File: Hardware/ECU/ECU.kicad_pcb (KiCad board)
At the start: 2 copper layers, 0 parts

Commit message: PCB
Platine Vernetzt
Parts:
- added A1: Pololu_Breakout_DRV8825, Module:Pololu_Breakout-16_15.2x20.3mm, F.Cu at (173.5, 128.5)
- added BT1: Battery_Cell, 2999:BAT_2999, F.Cu at (154.5, 72.0)
- added C10: 1uF, Capacitor_SMD:C_0805_2012Metric, F.Cu at (111.4, 138.5)
- added C11: 1uF, Capacitor_SMD:C_0805_2012Metric, F.Cu at (200.8, 106.7)
- added C12: 0.1uF, Capacitor_SMD:C_0805_2012Metric, F.Cu at (194.2, 93.6)
- added C13: 0.1uF, Capacitor_SMD:C_0805_2012Metric, F.Cu at (96.0, 40.7)
- added C14: 0.1uF, Capacitor_SMD:C_0805_2012Metric, F.Cu at (73.5, 47.5)
- added C15: 270nF, Capacitor_SMD:C_0805_2012Metric, F.Cu at (96.0, 45.7)
- added C16: 0.22uF, Capacitor_SMD:C_0805_2012Metric, F.Cu at (92.4, 39.6)
- added C17: 0.22uF, Capacitor_SMD:C_0805_2012Metric, F.Cu at (70.0, 51.5)
- added C18: 270nF, Capacitor_SMD:C_0805_2012Metric, F.Cu at (73.0, 40.5)
- added C20: 0.1uF, Capacitor_SMD:C_0805_2012Metric, F.Cu at (92.5, 52.2)
- added C21: 0.1uF, Capacitor_SMD:C_0805_2012Metric, F.Cu at (102.0, 59.1)
- added C23: 0.1uF, Capacitor_SMD:C_0805_2012Metric, F.Cu at (91.5, 47.1)
- added C24: 0.22uF, Capacitor_SMD:C_0805_2012Metric, F.Cu at (92.6, 56.1)
- added C25: 0.22uF, Capacitor_SMD:C_0805_2012Metric, F.Cu at (97.0, 65.2)
- added C26: 0.1uF, Capacitor_SMD:C_0805_2012Metric, F.Cu at (117.2, 46.2)
- added C27: 100uF, Capacitor_SMD:C_1206_3216Metric, F.Cu at (123.9, 47.5)
- added C28: 0.22uF, Capacitor_SMD:C_0805_2012Metric, F.Cu at (117.2, 49.2)
- added C29: 0.01uF, Capacitor_SMD:C_0805_2012Metric, F.Cu at (119.4, 66.8)
- added C3: 0.1uF, Capacitor_SMD:C_0805_2012Metric, F.Cu at (83.5, 122.0)
- added C30: 0.01uF, Capacitor_SMD:C_0805_2012Metric, F.Cu at (119.4, 69.8)
- added C31: 100uF, Capacitor_SMD:CP_Elec_6.3x7.7, F.Cu at (182.3, 136.7)
- added C32: 0.1uF, Capacitor_SMD:C_0805_2012Metric, F.Cu at (96.0, 74.5)
- added C33: 47uF, Capacitor_Tantalum_SMD:CP_EIA-3528-21_Kemet-B, F.Cu at (93.0, 74.5)
- added C34: 0.1uF, Capacitor_SMD:C_0805_2012Metric, F.Cu at (95.5, 96.8)
- added C35: 22uF, Capacitor_SMD:CP_Elec_4x5.4, F.Cu at (79.0, 98.3)
- added C36: 47uF, Capacitor_Tantalum_SMD:CP_EIA-3528-21_Kemet-B, F.Cu at (95.5, 99.5)
- added C37: 0.1uF, Capacitor_SMD:C_0805_2012Metric, F.Cu at (73.5, 98.3)
- added C38: 33uF, Capacitor_SMD:CP_Elec_6.3x7.7, F.Cu at (73.0, 83.0)
- added C39: 33uF, Capacitor_SMD:CP_Elec_6.3x7.7, F.Cu at (73.0, 75.5)
- added C4: 0.01uF, Capacitor_SMD:C_0805_2012Metric, F.Cu at (75.7, 139.3)
- added C40: 0.1uF, Capacitor_SMD:C_0805_2012Metric, F.Cu at (73.2, 88.0)
- added C41: 0.1uF, Capacitor_SMD:C_0805_2012Metric, F.Cu at (92.5, 34.7)
- added C5: 4700pF, Capacitor_SMD:C_0805_2012Metric, F.Cu at (72.7, 139.3)
- added C6: 1nF, Capacitor_SMD:C_0805_2012Metric, F.Cu at (115.4, 132.5)
- added C7: 0.01uF, Capacitor_SMD:C_0805_2012Metric, F.Cu at (111.4, 133.5)
- added C8: 1nF, Capacitor_SMD:C_0805_2012Metric, F.Cu at (107.4, 132.6)
- added C9: 0.1uF, Capacitor_SMD:C_0805_2012Metric, F.Cu at (111.4, 136.0)
- added D1: LED, LED_SMD:LED_0805_2012Metric, F.Cu at (206.8, 62.4)
- added D11: D, Diode_SMD:D_SOD-323, F.Cu at (198.8, 65.8)
- added D13: D, Diode_SMD:D_SOD-323, F.Cu at (206.8, 65.8)
- added D15: D, Diode_SMD:D_SOD-323, F.Cu at (194.8, 65.8)
- added D18: LED, LED_SMD:LED_0805_2012Metric, F.Cu at (206.8, 69.2)
- added D19: LED, LED_SMD:LED_0805_2012Metric, F.Cu at (194.8, 69.2)
- added D2: LED, LED_SMD:LED_0805_2012Metric, F.Cu at (202.8, 62.4)
- added D21: LED, LED_SMD:LED_0805_2012Metric, F.Cu at (198.8, 62.4)
- added D22: LED, LED_SMD:LED_0805_2012Metric, F.Cu at (194.8, 62.4)
- added D25: D, Diode_SMD:D_SOD-323, F.Cu at (194.3, 128.9)
- added D26: D, Diode_SMD:D_SOD-323, F.Cu at (190.3, 128.9)
- added D27: D_Schottky, Diode_SMD:D_PowerDI-123, F.Cu at (155.5, 123.7)
- added D28: D, Diode_SMD:D_SOD-323, F.Cu at (202.8, 128.9)
- added D29: D, Diode_SMD:D_SOD-323, F.Cu at (198.8, 128.9)
- added D30: D, Diode_SMD:D_SOD-323, F.Cu at (185.8, 128.9)
- added D31: D, Diode_SMD:D_SOD-323, F.Cu at (181.8, 128.9)
- added D32: D_TVS, Diode_SMD:D_SMB, F.Cu at (73.2, 69.5)
- added D33: D_Schottky, Diode_SMD:D_SMA_Handsoldering, F.Cu at (79.5, 62.5)
- added D34: LED, LED_SMD:LED_0805_2012Metric_Pad1.15x1.40mm_HandSolder, F.Cu at (108.0, 104.0)
- added D35: LED, LED_SMD:LED_0805_2012Metric_Pad1.15x1.40mm_HandSolder, F.Cu at (105.5, 104.0)
- added D36: LED, LED_SMD:LED_0805_2012Metric_Pad1.15x1.40mm_HandSolder, F.Cu at (103.0, 104.0)
- added D37: D_Schottky, Diode_SMD:D_PowerDI-123, F.Cu at (145.5, 75.7)
- added D5: LED, LED_SMD:LED_0805_2012Metric, F.Cu at (202.8, 69.2)
- added D7: LED, LED_SMD:LED_0805_2012Metric, F.Cu at (198.8, 69.2)
- added D9: D, Diode_SMD:D_SOD-323, F.Cu at (202.8, 65.8)
- added F1: Polyfuse, Fuse:Fuse_1812_4532Metric, F.Cu at (184.3, 106.2)
- added F2: Polyfuse, Fuse:Fuse_0603_1608Metric, F.Cu at (94.0, 103.0)
- added IC1: MAX9926UAEE_V+, Package_SO:QSOP-16_3.9x4.9mm_P0.635mm, F.Cu at (111.5, 126.9)
- added IC2: ZXMS6006DT8, ZXMS6006DT8TA:SOT153P700X170-8N, F.Cu at (192.3, 123.4)
- added IC3: ZXMS6006DT8, ZXMS6006DT8TA:SOT153P700X170-8N, F.Cu at (183.8, 123.4)
- added IC4: ZXMS6006DT8, ZXMS6006DT8TA:SOT153P700X170-8N, F.Cu at (200.8, 123.4)
- added J1: Conn_01x04, Connector_PinHeader_2.54mm:PinHeader_1x04_P2.54mm_Vertical, F.Cu at (127.0, 80.2)
- added J5: ~, connector:6437288-3, F.Cu at (206.0, 36.5)
- added JP2: Jumper_2_Open, Jumper:SolderJumper-2_P1.3mm_Open_Pad1.0x1.5mm, F.Cu at (79.4, 110.0)
- added JP3: Jumper_2_Open, Jumper:SolderJumper-2_P1.3mm_Open_Pad1.0x1.5mm, F.Cu at (79.4, 122.0)
- added JP4: Jumper_2_Open, Jumper:SolderJumper-2_P1.3mm_Open_Pad1.0x1.5mm, F.Cu at (96.8, 103.5)
- added Q1: Q_DUAL_NMOS_S1G1D2S2G2D1, Package_TO_SOT_SMD:SOT-363_SC-70-6, F.Cu at (79.4, 116.3)
- added Q2: Q_DUAL_NMOS_S1G1D2S2G2D1, Package_TO_SOT_SMD:SOT-363_SC-70-6, F.Cu at (123.7, 67.3)
- added Q3: Q_PNP_BCEC, Package_TO_SOT_SMD:SOT-223-3_TabPin2, F.Cu at (89.0, 99.0)
- added R10: 1k, Resistor_SMD:R_0805_2012Metric, F.Cu at (202.8, 58.9)
- added R13: 1k, Resistor_SMD:R_0805_2012Metric, F.Cu at (202.8, 72.7)
- added R15: 1k, Resistor_SMD:R_0805_2012Metric, F.Cu at (198.8, 72.7)
- added R17: 10k, Resistor_SMD:R_0805_2012Metric, F.Cu at (199.4, 82.1)
- added R20: 1k, Resistor_SMD:R_0805_2012Metric, F.Cu at (206.8, 72.7)
- added R21: 1k, Resistor_SMD:R_0805_2012Metric, F.Cu at (194.8, 72.7)
- added R23: 1k, Resistor_SMD:R_0805_2012Metric, F.Cu at (198.8, 58.9)
- added R24: 1k, Resistor_SMD:R_0805_2012Metric, F.Cu at (194.8, 58.9)
- added R27: 604R, Resistor_SMD:R_0805_2012Metric, F.Cu at (73.6, 50.0)
- added R28: 3.88k, Resistor_SMD:R_0805_2012Metric_Pad1.20x1.40mm_HandSolder, F.Cu at (75.0, 58.5)
- added R29: 470R, Resistor_SMD:R_0805_2012Metric, F.Cu at (96.0, 38.2)
- added R3: 1k, Resistor_SMD:R_0805_2012Metric, F.Cu at (79.4, 113.0)
- added R30: 2.4k, Resistor_SMD:R_0805_2012Metric, F.Cu at (96.1, 43.7)
- added R31: 470R, Resistor_SMD:R_0805_2012Metric, F.Cu at (73.6, 54.5)
- added R32: 1k, Resistor_SMD:R_0805_2012Metric, F.Cu at (73.0, 34.5)
- added R33: 2.49k, Resistor_SMD:R_0805_2012Metric, F.Cu at (96.4, 52.2)
- added R34: 2.49k, Resistor_SMD:R_0805_2012Metric, F.Cu at (96.5, 60.5)
- added R35: 470R, Resistor_SMD:R_0805_2012Metric, F.Cu at (96.0, 56.1)
- added R36: 470R, Resistor_SMD:R_0805_2012Metric, F.Cu at (93.1, 60.7)
- added R37: 0, Resistor_SMD:R_0805_2012Metric, F.Cu at (95.9, 48.2)
- added R38: 180k, Resistor_SMD:R_0805_2012Metric, F.Cu at (107.1, 37.0)
- added R39: 180k, Resistor_SMD:R_0805_2012Metric, F.Cu at (107.1, 40.0)
- added R4: 1k, Resistor_SMD:R_0805_2012Metric, F.Cu at (79.4, 119.5)
- added R40: 348k, Resistor_SMD:R_0805_2012Metric, F.Cu at (107.1, 42.9)
- added R41: 348k, Resistor_SMD:R_0805_2012Metric, F.Cu at (107.1, 45.9)
- added R42: 470R, Resistor_SMD:R_0805_2012Metric, F.Cu at (107.1, 48.8)
- added R43: 180k, Resistor_SMD:R_0805_2012Metric, F.Cu at (111.5, 37.0)
- added R44: 180k, Resistor_SMD:R_0805_2012Metric, F.Cu at (111.5, 40.0)
- added R45: 348k, Resistor_SMD:R_0805_2012Metric, F.Cu at (111.5, 42.9)
- added R46: 348k, Resistor_SMD:R_0805_2012Metric, F.Cu at (111.5, 45.9)
- added R47: 1k, Resistor_SMD:R_0805_2012Metric, F.Cu at (114.9, 56.4)
- added R48: 180k, Resistor_SMD:R_0805_2012Metric, F.Cu at (114.9, 59.4)
- added R49: 348k, Resistor_SMD:R_0805_2012Metric, F.Cu at (114.9, 62.3)
- added R5: 10k, Resistor_SMD:R_1206_3216Metric, F.Cu at (118.4, 137.0)
- added R50: 1k, Resistor_SMD:R_0805_2012Metric, F.Cu at (114.9, 65.3)
- added R51: 180k, Resistor_SMD:R_0805_2012Metric, F.Cu at (114.9, 68.2)
- added R52: 348k, Resistor_SMD:R_0805_2012Metric, F.Cu at (114.9, 71.2)
- added R53: 1k, Resistor_SMD:R_0805_2012Metric_Pad1.20x1.40mm_HandSolder, F.Cu at (191.3, 115.2)
- added R54: 1k, Resistor_SMD:R_0805_2012Metric_Pad1.20x1.40mm_HandSolder, F.Cu at (193.3, 115.2)
- added R55: 100k, Resistor_SMD:R_0805_2012Metric_Pad1.20x1.40mm_HandSolder, F.Cu at (189.3, 115.2)
- added R56: 100k, Resistor_SMD:R_0805_2012Metric_Pad1.20x1.40mm_HandSolder, F.Cu at (195.3, 115.2)
- added R57: 10k, Resistor_SMD:R_0805_2012Metric, F.Cu at (170.1, 49.5)
- added R58: 1k, Resistor_SMD:R_0805_2012Metric_Pad1.20x1.40mm_HandSolder, F.Cu at (183.3, 115.2)
- added R59: 1k, Resistor_SMD:R_0805_2012Metric_Pad1.20x1.40mm_HandSolder, F.Cu at (185.3, 115.2)
- added R6: 10k, Resistor_SMD:R_1206_3216Metric, F.Cu at (115.4, 137.0)
- added R60: 1k, Resistor_SMD:R_0805_2012Metric_Pad1.20x1.40mm_HandSolder, F.Cu at (203.2, 115.2)
- added R61: 1k, Resistor_SMD:R_0805_2012Metric_Pad1.20x1.40mm_HandSolder, F.Cu at (197.2, 115.2)
- added R62: 100k, Resistor_SMD:R_0805_2012Metric_Pad1.20x1.40mm_HandSolder, F.Cu at (181.3, 115.2)
- added R63: 100k, Resistor_SMD:R_0805_2012Metric_Pad1.20x1.40mm_HandSolder, F.Cu at (187.3, 115.2)
- added R64: 100k, Resistor_SMD:R_0805_2012Metric_Pad1.20x1.40mm_HandSolder, F.Cu at (201.2, 115.2)
- added R65: 100k, Resistor_SMD:R_0805_2012Metric_Pad1.20x1.40mm_HandSolder, F.Cu at (199.2, 115.2)
- added R66: 1k, Resistor_SMD:R_0805_2012Metric, F.Cu at (108.0, 99.6)
- added R67: 470R, Resistor_SMD:R_0805_2012Metric, F.Cu at (105.5, 99.6)
- added R68: 470R, Resistor_SMD:R_0805_2012Metric, F.Cu at (103.0, 99.6)
- added R69: 1k, Resistor_SMD:R_0805_2012Metric, F.Cu at (146.0, 71.1)
- added R7: 10k, Resistor_SMD:R_1206_3216Metric, F.Cu at (107.4, 137.0)
- added R70: 0, Resistor_SMD:R_0805_2012Metric, F.Cu at (96.0, 34.7)
- added R8: 10k, Resistor_SMD:R_1206_3216Metric, F.Cu at (104.4, 137.0)
- added R9: 1k, Resistor_SMD:R_0805_2012Metric, F.Cu at (206.8, 58.9)
- added SW1: SW_DPDT_x2, Misc:AYZ0202AGRLC, F.Cu at (93.5, 113.7)
- added SW2: SW_DPDT_x2, Misc:AYZ0202AGRLC, F.Cu at (93.0, 137.5)
- added SW3: SW_DIP_x02, Button_Switch_SMD:SW_DIP_SPSTx02_Slide_9.78x7.26mm_W8.61mm_P2.54mm, F.Cu at (74.2, 130.3)
- added SW4: SW_DPDT_x2, Misc:AYZ0202AGRLC, F.Cu at (192.8, 100.5)
- added U1: Teensy4.1, kicad:Teensy41, F.Cu at (139.0, 112.0)
- added U12: LMV324LIDT, Package_SO:SOIC-14_3.9x8.7mm_P1.27mm, F.Cu at (125.3, 40.7)
- added U13: SP720, Package_SO:SOIC-16_3.9x9.9mm_P1.27mm, F.Cu at (83.0, 42.0)
- added U14: LMV324LIDT, Package_SO:SOIC-14_3.9x8.7mm_P1.27mm, F.Cu at (121.8, 58.7)
- added U15: MC33814, Package_QFP:LQFP-48-1EP_7x7mm_P0.5mm_EP3.6x3.6mm_ThermalVias, F.Cu at (93.3, 86.0)
- added U16: TC4424A, Package_SO:SOIC-8_3.9x4.9mm_P1.27mm, F.Cu at (105.5, 85.0)
- added U17: W25Q32JVSS, Package_SO:SOIC-8_5.3x5.3mm_P1.27mm, F.Cu at (156.0, 95.0)
- added U3: 74AHC1G32, Package_TO_SOT_SMD:SOT-353_SC-70-5, F.Cu at (125.0, 120.0)
- added U4: ADXL343, Package_LGA:LGA-14_3x5mm_P0.8mm_LayoutBorder1x6y, F.Cu at (123.5, 124.0)
- added U5: TC4424A, Package_SO:SOIC-8_3.9x4.9mm_P1.27mm, F.Cu at (201.2, 77.7)
- added U7: MC33810, IC_Automotive:SOIC32-P0.65-33N, F.Cu at (201.3, 89.1)
- added U9: TC4424A, Package_SO:SOIC-8_3.9x4.9mm_P1.27mm, F.Cu at (201.0, 99.6)
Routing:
- net GND: track 0.00 -> 688.5 mm, vias 0 -> 19
- net 12V-SW: track 0.00 -> 250.8 mm, vias 0 -> 10
- net +3V3: track 0.00 -> 237.8 mm, vias 0 -> 6
- net +5V: track 0.00 -> 218.1 mm, vias 0 -> 14
- net SCLK: track 0.00 -> 190.6 mm, vias 0 -> 12
- net MOSI: track 0.00 -> 175.9 mm, vias 0 -> 9
- net IDLE-OUT: track 0.00 -> 172.1 mm, vias 0 -> 2
- net MISO: track 0.00 -> 171.3 mm, vias 0 -> 10
- net SPARE2-OUT: track 0.00 -> 154.2 mm, vias 0 -> 2
- net SPARE1-OUT: track 0.00 -> 153.3 mm, vias 0 -> 3
- net CAM-IN-: track 0.00 -> 142.4 mm, vias 0 -> 5
- net MCU-A5: track 0.00 -> 129.9 mm, vias 0 -> 4
- net CAM-IN+: track 0.00 -> 129.4 mm, vias 0 -> 5
- net CRANK-IN+: track 0.00 -> 120.3 mm, vias 0 -> 4
- net BOOST-OUT: track 0.00 -> 120.2 mm, vias 0 -> 3
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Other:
- board outline added: 148 x 111.5 mm

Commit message: PCB V0.1
Erste Iteration der PCB vernetzt
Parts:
- moved R29 35.3 mm to (130.6, 45.0)
- moved C13 35.2 mm to (130.6, 47.0)
- moved U12 30.3 mm to (95.0, 41.5)
- moved Q2 29.7 mm to (125.5, 37.6)
- moved R51 29.7 mm to (130.6, 43.0)
- moved C23 26.4 mm to (115.5, 36.0), turned to 180 degrees
- moved R37 24.1 mm to (115.4, 34.0)
- moved R48 24.1 mm to (130.5, 41.0)
- moved R70 19.2 mm to (114.4, 40.0)
- moved C41 18.9 mm to (110.5, 40.0)
- moved R50 17.3 mm to (127.1, 53.0)
- moved C15 17.2 mm to (90.5, 62.0)
- moved R30 16.0 mm to (93.9, 59.5), turned to 180 degrees
- moved C30 15.9 mm to (125.0, 55.0)
- moved C25 15.4 mm to (91.0, 51.0)
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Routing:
- net GND: track 688.5 -> 1013.6 mm, vias 19 -> 35
- net ADC-Clamp-5: track 0.00 -> 236.1 mm, vias 0 -> 6
- net ADC-Clamp-6: track 0.00 -> 224.4 mm, vias 0 -> 4
- net ADC-Clamp-4: track 0.00 -> 220.4 mm, vias 0 -> 6
- net ADC-Clamp-7: track 0.00 -> 210.9 mm, vias 0 -> 4
- net ADC-Clamp-12: track 0.00 -> 209.2 mm, vias 0 -> 8
- net ADC-Clamp-3: track 0.00 -> 195.9 mm, vias 0 -> 4
- net ADC-Clamp-11: track 0.00 -> 184.7 mm, vias 0 -> 6
- net +3V3: track 237.8 -> 415.3 mm, vias 6 -> 17
- net ADC-Clamp-13: track 0.00 -> 175.2 mm, vias 0 -> 4
- net ADC-Clamp-14: track 0.00 -> 171.1 mm, vias 0 -> 5
- net MCU-A0: track 0.00 -> 157.6 mm, vias 0 -> 5
- net MCU-A1: track 0.00 -> 148.5 mm, vias 0 -> 5
- net MCU-A9: track 0.00 -> 110.4 mm, vias 0 -> 6
- net MCU-A8: track 0.00 -> 106.3 mm, vias 0 -> 6
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
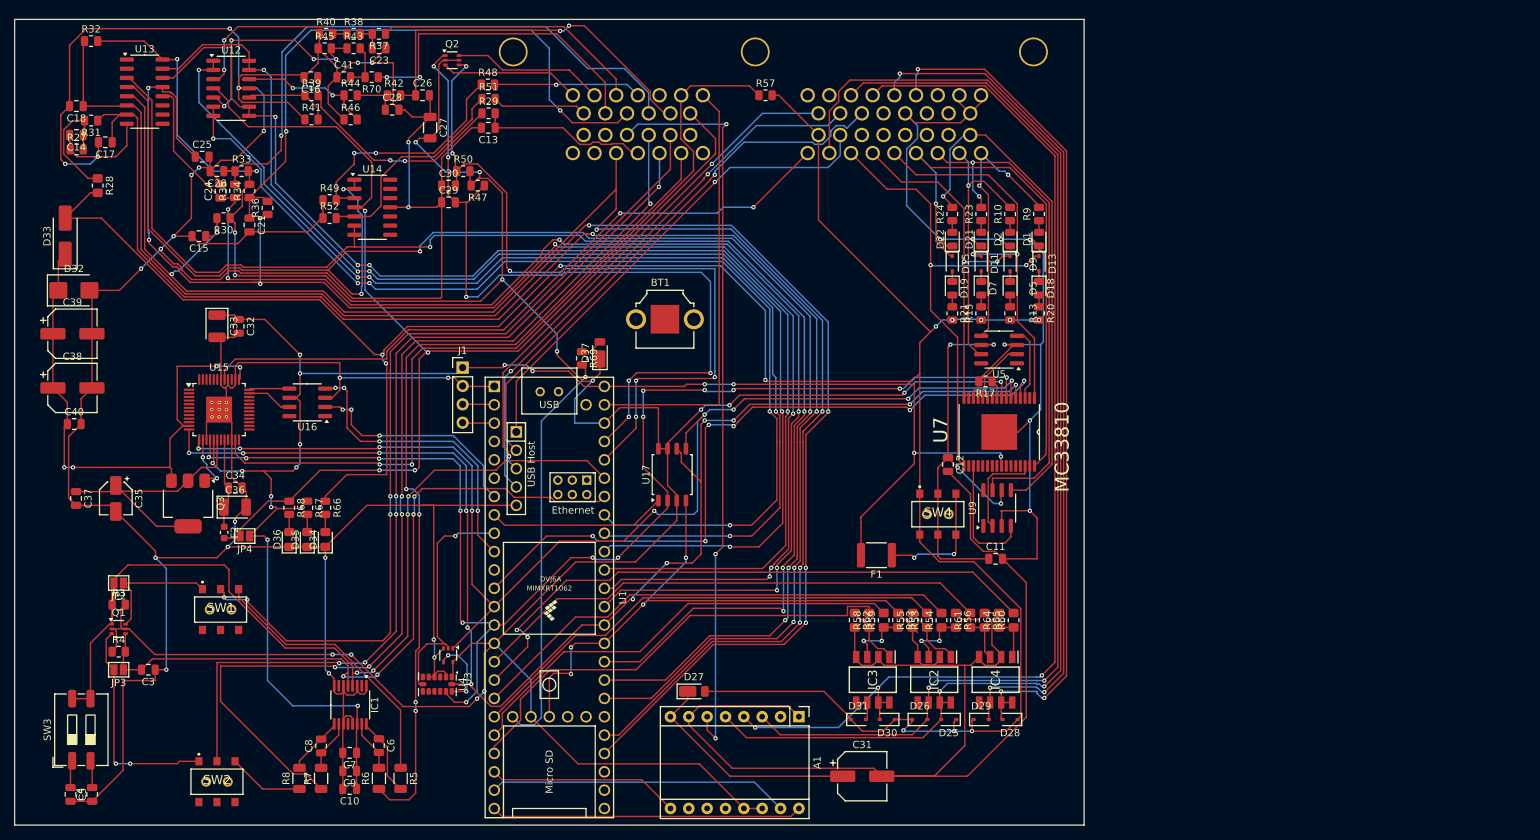
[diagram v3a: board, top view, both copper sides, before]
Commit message: Add new footprint for TO-220AB MOSFET (IRFB4110PBF)
- Created a new KiCad module for the TO254P483X1016X1994-3P footprint.
- Included necessary graphical elements such as courtyard, fabrication, and silkscreen layers.
- Defined pads for through-hole connections with appropriate dimensions and drill sizes.
- Added a 3D model reference for the IRFB4110PBF component.
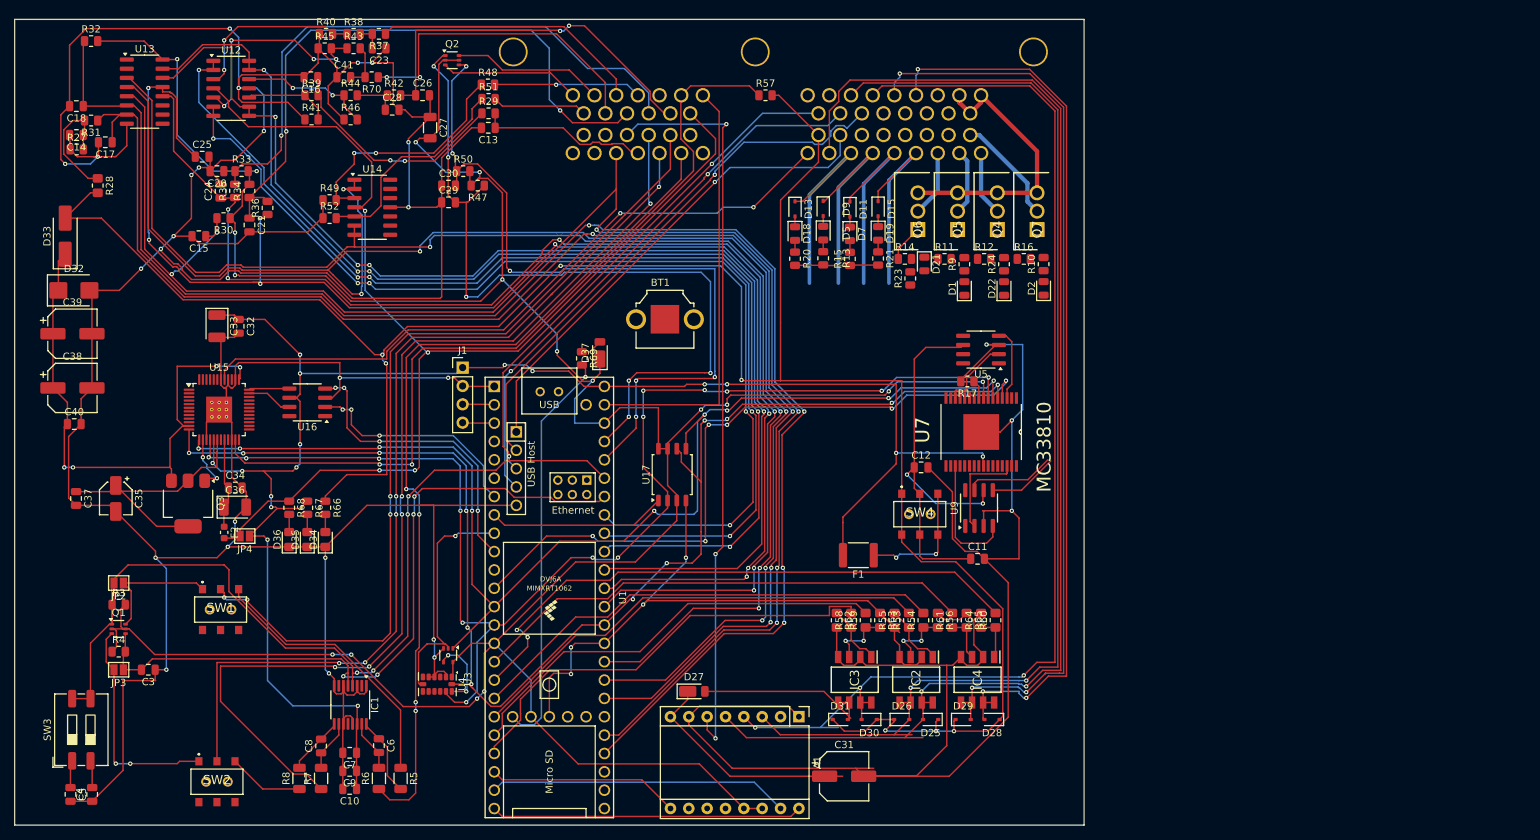
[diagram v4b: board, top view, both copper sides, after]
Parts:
- added Q4: IRFB4110PBF, LIB_IRFB4110PBF:TO254P483X1016X1994-3P, F.Cu at (201.0, 61.1)
- added Q5: IRFB4110PBF, LIB_IRFB4110PBF:TO254P483X1016X1994-3P, F.Cu at (195.5, 61.1)
- added Q6: IRFB4110PBF, LIB_IRFB4110PBF:TO254P483X1016X1994-3P, F.Cu at (190.0, 61.1)
- added Q7: IRFB4110PBF, LIB_IRFB4110PBF:TO254P483X1016X1994-3P, F.Cu at (206.5, 61.1)
- added R11: 33, Resistor_SMD:R_0805_2012Metric, F.Cu at (193.7, 65.2)
- added R12: 33, Resistor_SMD:R_0805_2012Metric, F.Cu at (199.2, 65.2)
- added R14: 33, Resistor_SMD:R_0805_2012Metric, F.Cu at (188.2, 65.2)
- added R16: 33, Resistor_SMD:R_0805_2012Metric, F.Cu at (204.7, 65.2)
- moved D13 34.6 mm to (173.0, 58.2)
- moved D18 34.6 mm to (173.0, 61.6)
- moved R20 34.6 mm to (173.0, 65.1)
- moved D5 27.0 mm to (176.9, 61.6)
- moved D9 27.0 mm to (176.9, 58.2)
- moved R13 27.0 mm to (176.9, 65.1)
- moved D7 19.7 mm to (180.6, 61.7)
- moved R15 19.7 mm to (180.6, 65.1)
- moved D11 19.7 mm to (180.6, 58.3)
- moved R23 13.3 mm to (188.9, 67.8)
- moved D19 12.8 mm to (184.5, 61.6)
- moved D15 12.8 mm to (184.5, 58.2)
- moved R21 12.8 mm to (184.5, 65.1)
- moved R9 12.4 mm to (196.4, 65.9)
- moved D1 12.4 mm to (196.4, 69.2)
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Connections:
- R10 pad 2: IGN2 -> Net-(U5-OUT_A)
- R23 pad 2: IGN3 -> Net-(U9-OUT_A)
- R24 pad 2: IGN4 -> Net-(U9-OUT_B)
- R69 pad 1: Net-(D37-A) -> VBat
- R69 pad 2: VBat -> Net-(D37-A)
- R9 pad 2: IGN1 -> Net-(U5-OUT_B)
- U5 pad 5: IGN1 -> Net-(U5-OUT_B)
- U5 pad 7: IGN2 -> Net-(U5-OUT_A)
- U9 pad 5: IGN4 -> Net-(U9-OUT_B)
- U9 pad 7: IGN3 -> Net-(U9-OUT_A)
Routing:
- net IGN3: track 71.3 -> 9.18 mm, vias 2 -> 0
- net IGN4: track 71.3 -> 15.1 mm, vias 1 -> 0
- net INJ4: track 74.3 -> 28.4 mm, vias 1 -> 0
- net INJ1: track 67.7 -> 30.9 mm, vias 2 -> 0
- net GND: track 1013.6 -> 979.5 mm, vias 35 -> 31
- net IGN1: track 37.6 -> 8.97 mm, vias 2 -> 0
- net IGN2: track 36.8 -> 9.04 mm, vias 1 -> 0
- net INJ3: track 55.2 -> 29.0 mm, vias 2 -> 0
- net INJ2: track 48.7 -> 29.6 mm, vias 2 -> 0
- net Net-(U9-OUT_A): track 0.00 -> 12.5 mm
- net 12V-SW: track 353.0 -> 342.4 mm, vias 12 -> 7
- net Net-(U9-OUT_B): track 0.00 -> 9.71 mm
- net BOOST-OUT: track 120.2 -> 126.5 mm
- net FAN-OUT: track 118.0 -> 124.1 mm
- net IDLE-OUT: track 172.1 -> 178.2 mm
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
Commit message: PCB v0.2
leiterbahndicke updated
Clutch input rework
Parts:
- added D3: 1N4148WT, Diode_SMD:D_SOD-523, F.Cu at (79.2, 34.0)
- moved R10 13.1 mm to (194.4, 67.8)
- moved D2 11.5 mm to (196.4, 65.8), turned to -90 degrees
- moved D22 6.45 mm to (207.4, 65.8), turned to -90 degrees
- moved D1 6.44 mm to (201.9, 65.8), turned to -90 degrees
- moved R24 3.98 mm to (205.4, 67.8)
- moved R9 3.96 mm to (199.9, 67.8)
- moved BT1 0.10 mm to (155.1, 73.5)
- moved R16 0.07 mm to (204.7, 65.1)
- moved R12 0.06 mm to (199.2, 65.1)
- moved R11 0.05 mm to (193.7, 65.1)
- moved R14 0.05 mm to (188.2, 65.1)
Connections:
- net SPARE1_Sensor renamed Gear_Position
- net VVT-OUT renamed SPARE2_OUT
- J5 pad 19: /Conntectors/Starter Relay Input -> Clutch_in
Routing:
- net GND: track 979.5 -> 1211.3 mm, vias 31 -> 36
- net Clutch_in: track 0.00 -> 126.2 mm, vias 0 -> 1
- net MC33814-CS: track 0.00 -> 46.7 mm, vias 0 -> 1
- net Net-(U9-OUT_A): track 12.5 -> 57.9 mm
- net INJ4: track 28.4 -> 69.4 mm, vias 0 -> 1
- net INJ1: track 30.9 -> 66.7 mm, vias 0 -> 1
- net INJ3: track 29.0 -> 62.0 mm, vias 0 -> 1
- net Net-(U9-OUT_B): track 9.71 -> 39.9 mm
- net VBat: track 56.4 -> 79.8 mm
- net INJ2: track 29.6 -> 52.4 mm, vias 0 -> 1
- net Net-(U5-OUT_A): track 0.62 -> 17.2 mm, vias 0 -> 2
- net Net-(U5-OUT_B): track 0.00 -> 13.0 mm, vias 0 -> 2
- net O2-Heater: track 103.5 -> 97.6 mm, vias 4 -> 3
- net Net-(Q5-G): track 0.00 -> 5.14 mm
- net Net-(Q4-G): track 0.00 -> 5.14 mm
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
